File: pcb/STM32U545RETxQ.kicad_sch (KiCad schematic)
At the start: 14 parts, among them U3 STM32U545RETxQ

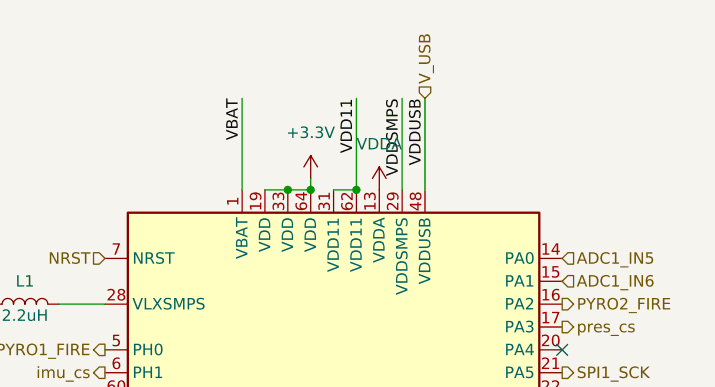
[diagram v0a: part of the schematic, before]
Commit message: Updated Control Module Test bed schematics
Added Test points for Pyro controllers, Micro SD, and USB-C

Connected VDDUSB to 3.3V and not Vusb
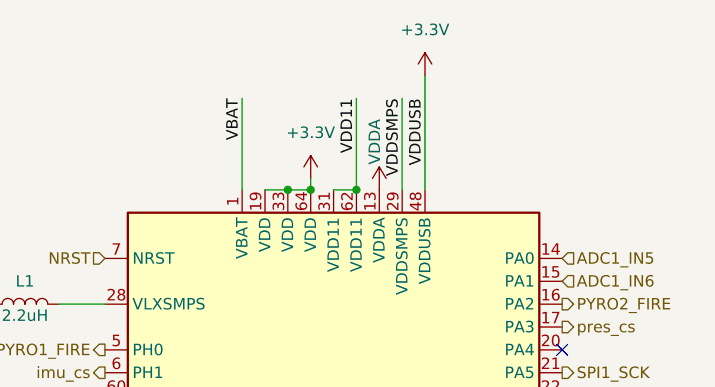
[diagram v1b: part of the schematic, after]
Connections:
- net V_USB is gone; now on net +3.3V: C15.1, U3.48 (VDDUSB)
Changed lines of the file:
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@@
 	(wire
 		(pts
-			(xy 168.91 40.64) (xy 168.91 50.8)
+			(xy 168.91 38.1) (xy 168.91 50.8)
 		)
 		(stroke
@@
 		(shape input)
 		(at 184.15 58.42 0)
-		(effects
-			(font
-				(size 1.27 1.27)
-			)
-			(justify left)
-		)
-	)
-	(hierarchical_label "V_USB"
-		(shape input)
-		(at 168.91 40.64 90)
 		(effects
 			(font
@@
 	)
 	(symbol
+		(lib_id "power:+3.3V")
+		(at 168.91 38.1 0)
+		(unit 1)
+		(exclude_from_sim no)
+		(in_bom yes)
+		(on_board yes)
+		(dnp no)
+		(fields_autoplaced yes)
+		(property "Reference" "#PWR056"
+			(at 168.91 41.91 0)
+			(effects
+				(font
+					(size 1.27 1.27)
+				)
+				(hide yes)
+			)
+		)
+		(property "Value" "+3.3V"
+			(at 168.91 33.02 0)
+			(effects
+				(font
+					(size 1.27 1.27)
+				)
+			)
+		)
+		(property "Footprint" ""
+			(at 168.91 38.1 0)
+			(effects
+				(font
+					(size 1.27 1.27)
+				)
+				(hide yes)
+			)
+		)
+		(property "Datasheet" ""
+			(at 168.91 38.1 0)
+			(effects
+				(font
+					(size 1.27 1.27)
+				)
+				(hide yes)
+			)
+		)
+		(property "Description" "Power symbol creates a global label with name \"+3.3V\""
+			(at 168.91 38.1 0)
+			(effects
+				(font
+					(size 1.27 1.27)
+				)
+				(hide yes)
+			)
+		)
+		(pin "1"
+		)
+		(instances
+			(project "control-module"
+				(path "/ba7b4294-8d75-4b9e-892f-fb52727887ec/646bb59c-dea9-4304-8415-d4c1819f029f"
+					(reference "#PWR056")
+					(unit 1)
+				)
+			)
+		)
+	)
+	(symbol
 		(lib_name "C_2")
 		(lib_id "Device:C")
@@
 		(on_board yes)
 		(dnp no)
-		(fields_autoplaced yes)
 		(property "Reference" "#PWR074"
 			(at 163.83 54.61 0)
@@
 		)
 		(property "Value" "VDDA"
-			(at 163.83 45.72 0)
-			(effects
-				(font
+			(at 163.322 45.466 90)
+			(effects
+				(font

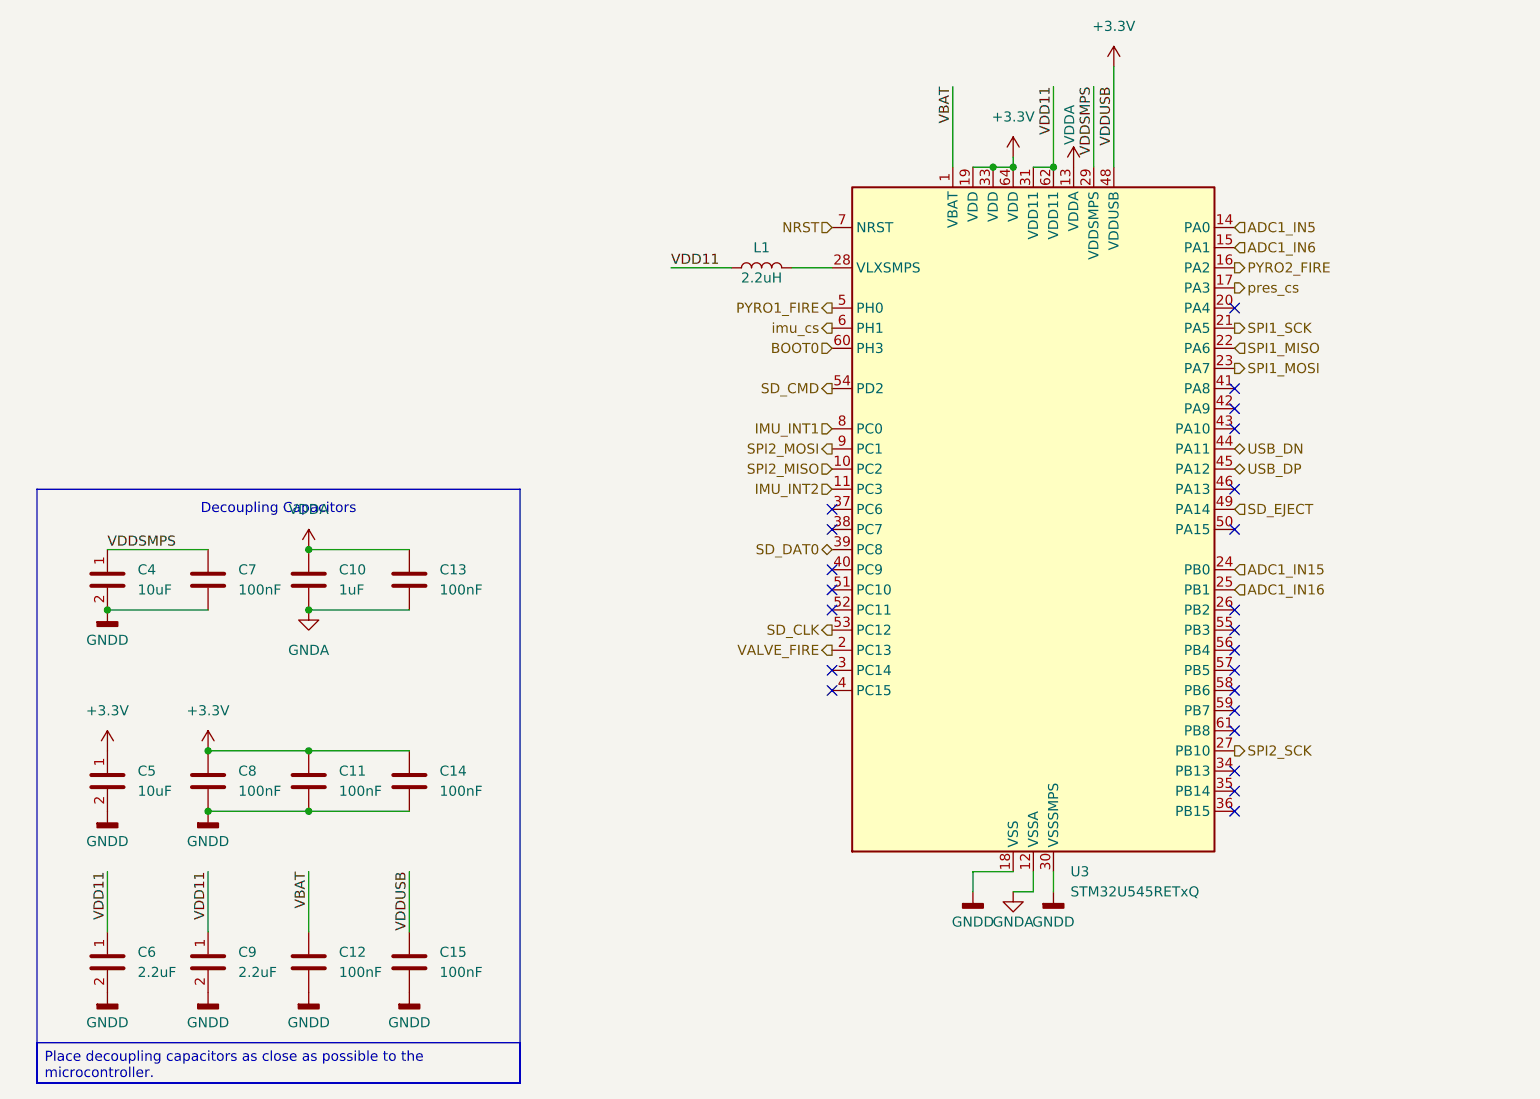
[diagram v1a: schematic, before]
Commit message: Added more testpoints
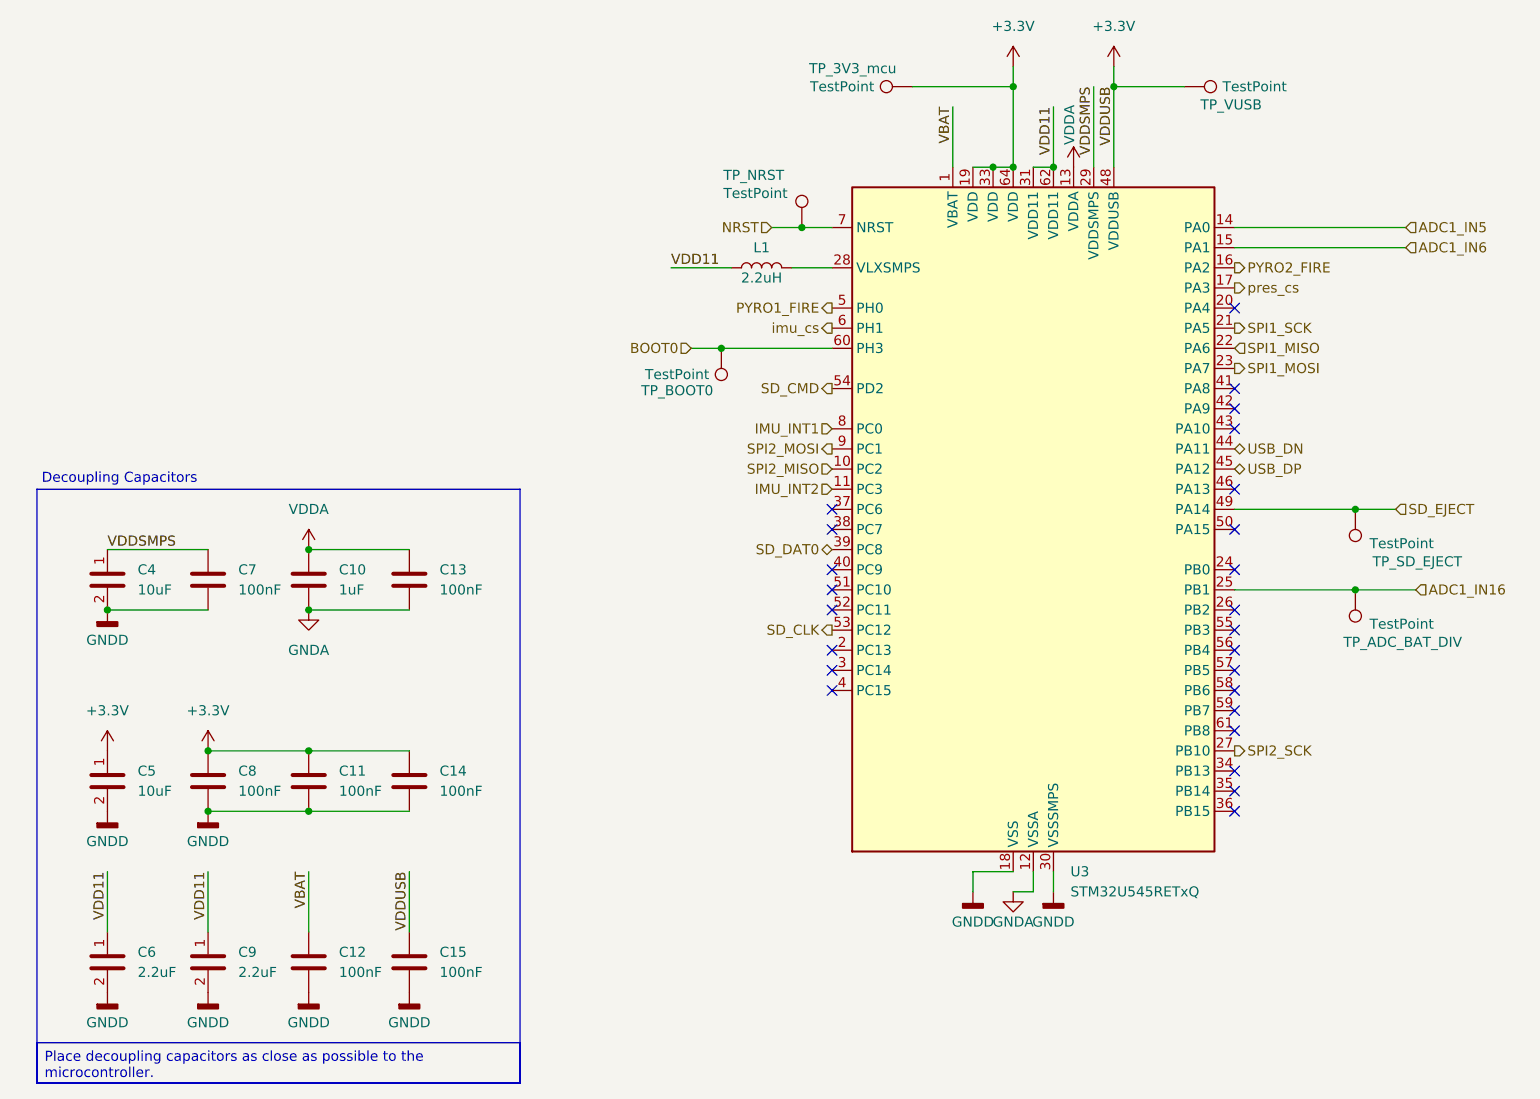
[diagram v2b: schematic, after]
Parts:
- added TP_3V3_mcu, TP_ADC_BAT_DIV, TP_BOOT0, TP_NRST, TP_SD_EJECT, TP_VUSB: TestPoint, TestPoint:TestPoint_Loop_D2.54mm_Drill1.5mm_Beaded, symbol Connector:TestPoint
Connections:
- net +3.3V: now also TP_3V3_mcu.1, TP_VUSB.1
- net ADC1_IN16: now also TP_ADC_BAT_DIV.1
- net BOOT0: now also TP_BOOT0.1
- net NRST: now also TP_NRST.1
- net SD_EJECT: now also TP_SD_EJECT.1
- net ADC1_IN15: no longer names the net of U3.24 (PB0)
- net VALVE_FIRE: no longer names the net of U3.2 (PC13)
- no-connect marks 23 -> 25
